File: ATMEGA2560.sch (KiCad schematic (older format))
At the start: 3 parts

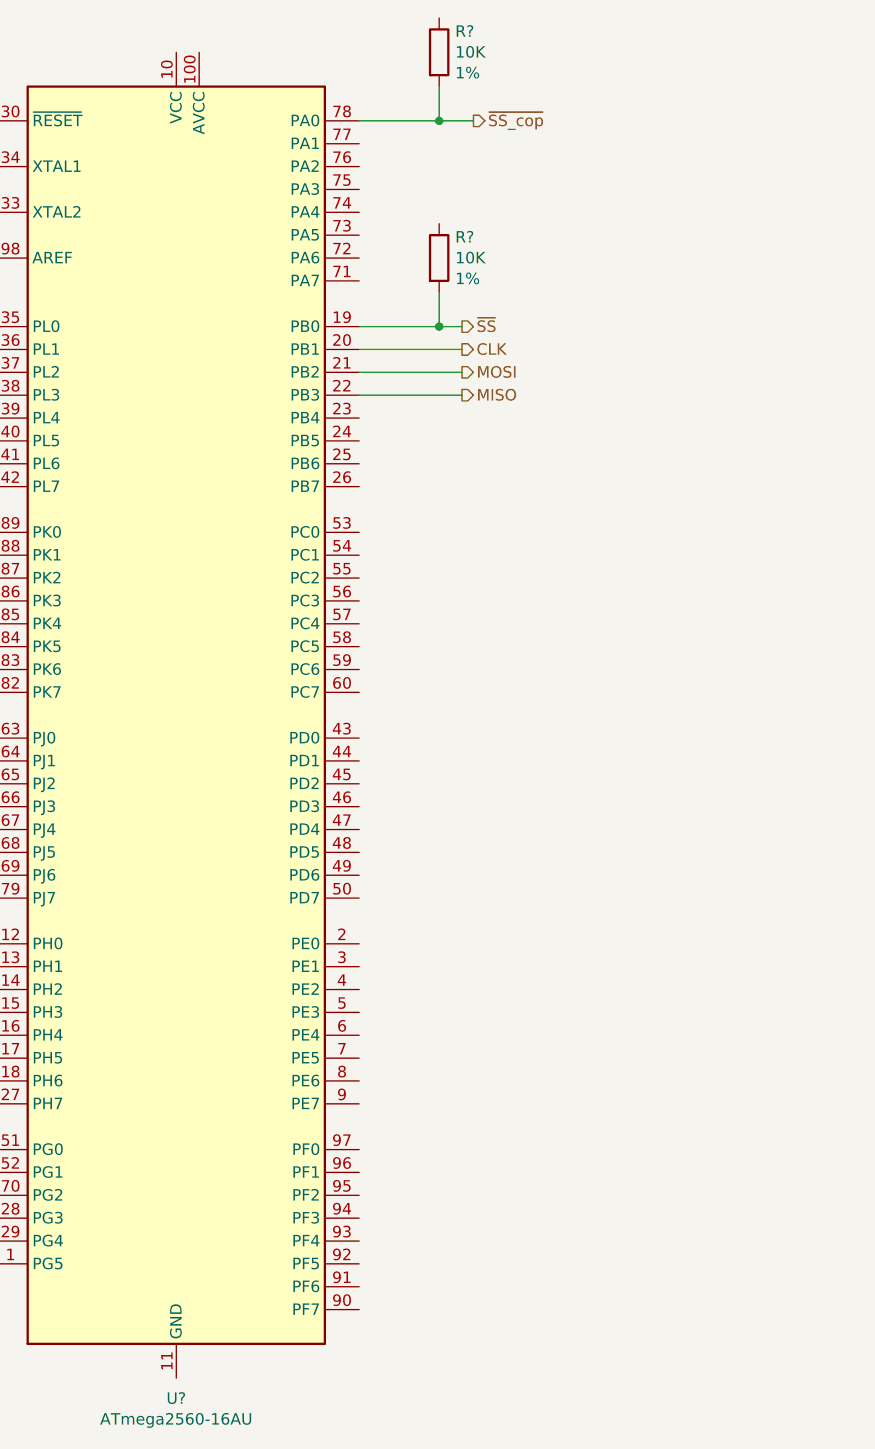
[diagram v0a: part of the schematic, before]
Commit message: Added all stepper circuits. Adding SPI bus to top level sheet. Opened up layout to check connectivity. Errors with footprint libs
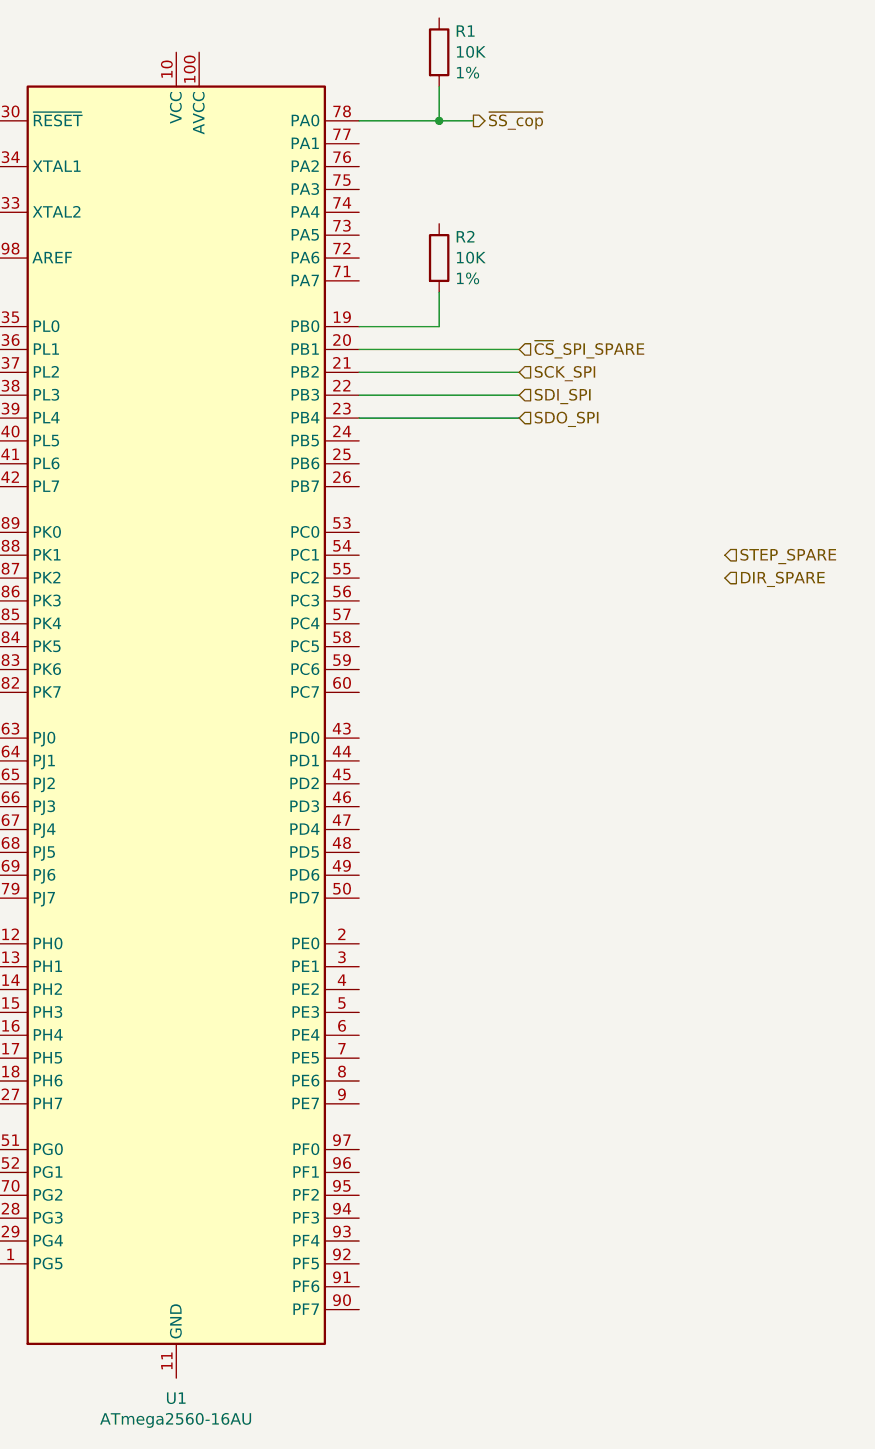
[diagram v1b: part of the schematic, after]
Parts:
- gave numbers to parts that had none: 3
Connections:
- net SDO_SPI: now reaches U1.23 (PB4)
- net CLK renamed ~CS~_SPI_SPARE
- net MISO renamed SDI_SPI
- net MOSI renamed SCK_SPI
- net ~SS: no longer names the net of R2.2, U1.19 (PB0)
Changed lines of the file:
@@
 EESchema Schematic File Version 4
-LIBS:bountifulHarvest-cache
-EELAYER 26 0
+EELAYER 30 0
 EELAYER END
 $Descr A4 11693 8268
 encoding utf-8
-Sheet 2 6
+Sheet 2 7
 Title ""
 Date ""
@@
 $EndDescr
 $Comp
-L bountifulHarvest-rescue:ATmega2560-16AU-MCU_Microchip_ATmega U?
+L bountifulHarvest-rescue:ATmega2560-16AU-MCU_Microchip_ATmega U1
 U 1 1 5EE66806
 P 4500 4250
-F 0 "U?" H 4500 1261 50  0000 C CNN
+F 0 "U1" H 4500 1261 50  0000 C CNN
 F 1 "ATmega2560-16AU" H 4500 1170 50  0000 C CNN
 F 2 "Package_QFP:TQFP-100_14x14mm_P0.5mm" H 4500 4250 50  0001 C CIN
@@
 	5300 1650 5650 1650
 $Comp
-L Device:R R?
+L Device:R R1
 U 1 1 5EE73D0C
 P 5650 1350
-F 0 "R?" H 5720 1441 50  0000 L CNN
+F 0 "R1" H 5720 1441 50  0000 L CNN
 F 1 "10K" H 5720 1350 50  0000 L CNN
 F 2 "" V 5580 1350 50  0001 C CNN
@@
 Wire Wire Line
 	5650 1650 5800 1650
-Text HLabel 5750 2850 2    50   Output ~ 0
-MISO
-Text HLabel 5750 2750 2    50   Output ~ 0
-MOSI
-Text HLabel 5750 2650 2    50   Output ~ 0
-CLK
-Text HLabel 5750 2550 2    50   Output ~ 0
-~SS
 $Comp
-L Device:R R?
+L Device:R R2
 U 1 1 5EE7AE50
 P 5650 2250
-F 0 "R?" H 5720 2341 50  0000 L CNN
+F 0 "R2" H 5720 2341 50  0000 L CNN
 F 1 "10K" H 5720 2250 50  0000 L CNN
 F 2 "" V 5580 2250 50  0001 C CNN
@@
 	5300 2550 5650 2550
 Wire Wire Line
-	5300 2650 5750 2650
+	5650 2400 5650 2550
+Text HLabel 6000 2650 2    50   Input ~ 0
+~CS~_SPI_SPARE
+Text HLabel 6000 2750 2    50   Input ~ 0
+SCK_SPI
+Text HLabel 6000 2850 2    50   Input ~ 0
+SDI_SPI
+Text HLabel 6000 2950 2    50   Input ~ 0
+SDO_SPI
+Text HLabel 6900 3550 2    50   Input ~ 0
+STEP_SPARE
+Text HLabel 6900 3650 2    50   Input ~ 0
+DIR_SPARE
 Wire Wire Line
-	5300 2750 5750 2750
+	5300 2650 6000 2650
 Wire Wire Line
-	5300 2850 5750 2850
+	6000 2750 5300 2750
 Wire Wire Line
-	5650 2400 5650 2550
-Connection ~ 5650 2550
+	5300 2850 6000 2850
 Wire Wire Line
-	5650 2550 5750 2550
+	6000 2950 5300 2950
 $EndSCHEMATC

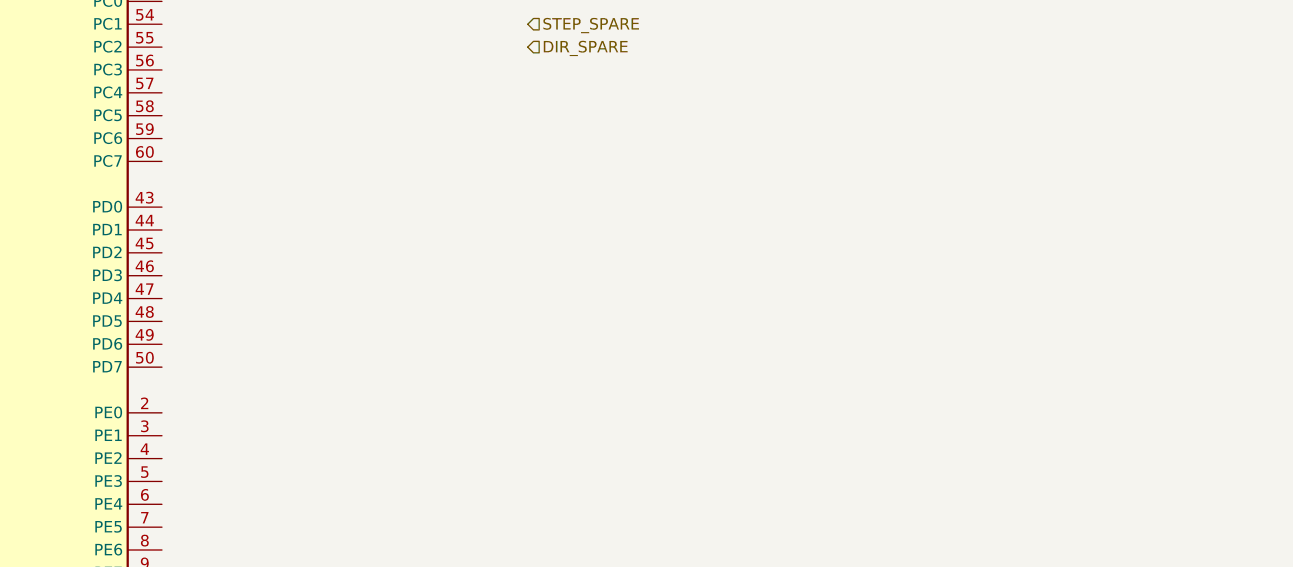
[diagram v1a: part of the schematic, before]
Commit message: Updated bus connections between drivers at ATMega
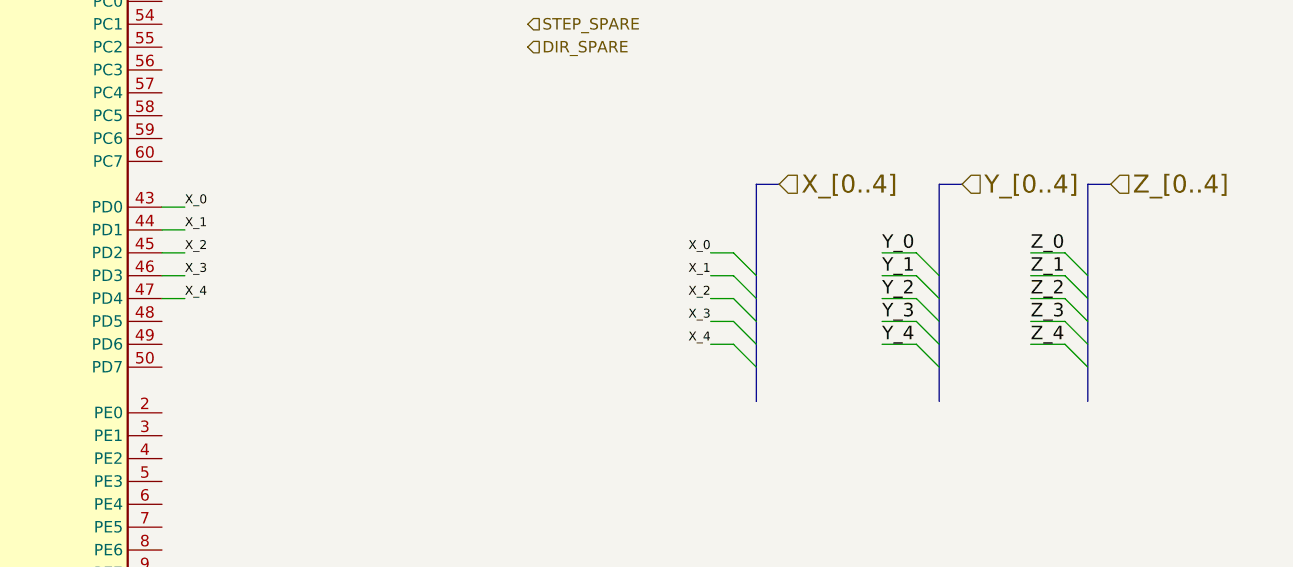
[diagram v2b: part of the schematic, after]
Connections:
- net X_0: now reaches U1.43 (PD0)
- net X_1: now reaches U1.44 (PD1)
- net X_2: now reaches U1.45 (PD2)
- net X_3: now reaches U1.46 (PD3)
- net X_4: now reaches U1.47 (PD4)
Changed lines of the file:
@@
 EESchema Schematic File Version 4
-EELAYER 30 0
+LIBS:bountifulHarvest-cache
+EELAYER 26 0
 EELAYER END
 $Descr A4 11693 8268
 encoding utf-8
-Sheet 2 7
+Sheet 6 7
 Title ""
 Date ""
@@
 Wire Wire Line
 	6000 2950 5300 2950
+Wire Wire Line
+	7700 4550 7800 4550
+Wire Wire Line
+	7700 4650 7800 4650
+Wire Wire Line
+	7700 4750 7800 4750
+Wire Wire Line
+	7700 4850 7800 4850
+Wire Wire Line
+	7700 4950 7800 4950
+Text Label 7700 4550 2    39   ~ 0
+X_0
+Text Label 7700 4650 2    39   ~ 0
+X_1
+Text Label 7700 4750 2    39   ~ 0
+X_2
+Text Label 7700 4850 2    39   ~ 0
+X_3
+Text Label 7700 4950 2    39   ~ 0
+X_4
+Entry Wire Line
+	7800 4550 7900 4650
+Entry Wire Line
+	7800 4650 7900 4750
+Entry Wire Line
+	7800 4750 7900 4850
+Entry Wire Line
+	7800 4850 7900 4950
+Entry Wire Line
+	7800 4950 7900 5050
+Wire Bus Line
+	7900 4250 8000 4250
+Wire Wire Line
+	5400 4350 5300 4350
+Wire Wire Line
+	5400 4450 5300 4450
+Wire Wire Line
+	5400 4550 5300 4550
+Wire Wire Line
+	5400 4650 5300 4650
+Wire Wire Line
+	5400 4750 5300 4750
+Text Label 5400 4350 0    39   ~ 0
+X_0
+Text Label 5400 4450 0    39   ~ 0
+X_1
+Text Label 5400 4550 0    39   ~ 0
+X_2
+Text Label 5400 4650 0    39   ~ 0
+X_3
+Text Label 5400 4750 0    39   ~ 0
+X_4
+Text HLabel 8000 4250 2    79   Input ~ 0
+X_[0..4]
+Entry Wire Line
+	8600 4550 8700 4650
+Entry Wire Line
+	8600 4650 8700 4750
+Entry Wire Line
+	8600 4750 8700 4850
+Entry Wire Line
+	8600 4850 8700 4950
+Entry Wire Line
+	8600 4950 8700 5050
+Text HLabel 8800 4250 2    79   Input ~ 0
+Y_[0..4]
+Wire Bus Line
+	8700 4250 8800 4250
+Entry Wire Line
+	9250 4550 9350 4650
+Entry Wire Line
+	9250 4650 9350 4750
+Entry Wire Line
+	9250 4750 9350 4850
+Entry Wire Line
+	9250 4850 9350 4950
+Entry Wire Line
+	9250 4950 9350 5050
+Text HLabel 9450 4250 2    79   Input ~ 0
+Z_[0..4]
+Wire Bus Line
+	9350 4250 9450 4250
+Text Label 8450 4550 0    59   ~ 0
+Y_0
+Text Label 8450 4650 0    59   ~ 0
+Y_1
+Text Label 8450 4750 0    59   ~ 0
+Y_2
+Text Label 8450 4850 0    59   ~ 0
+Y_3
+Text Label 8450 4950 0    59   ~ 0
+Y_4
+Wire Wire Line
+	8600 4550 8450 4550
+Wire Wire Line
+	8600 4650 8450 4650
+Wire Wire Line
+	8600 4750 8450 4750
+Wire Wire Line
+	8600 4850 8450 4850
+Wire Wire Line
+	8600 4950 8450 4950
+Text Label 9100 4550 0    59   ~ 0
+Z_0
+Text Label 9100 4650 0    59   ~ 0
+Z_1
+Text Label 9100 4750 0    59   ~ 0
+Z_2
+Text Label 9100 4850 0    59   ~ 0
+Z_3
+Text Label 9100 4950 0    59   ~ 0
+Z_4
+Wire Wire Line
+	9100 4550 9250 4550
+Wire Wire Line
+	9100 4650 9250 4650
+Wire Wire Line
+	9100 4750 9250 4750
+Wire Wire Line
+	9100 4850 9250 4850
+Wire Wire Line
+	9100 4950 9250 4950
+Wire Bus Line
+	7900 4250 7900 5200
+Wire Bus Line
+	8700 4250 8700 5200
+Wire Bus Line
+	9350 4250 9350 5200
 $EndSCHEMATC

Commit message: Fixed X,Y,Z driver bus connection. set up spare and X2
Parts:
- U1: Manufacturer P/N (none) -> ATMEGA2560-16AUR; Vendor P/N (none) -> ATMEGA2560-16AURCT-ND
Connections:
- net labels removed: DIR_SPARE, STEP_SPARE, ~CS~_SPI_SPARE
- wire segments 29 -> 38
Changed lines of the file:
@@
 $Descr A4 11693 8268
 encoding utf-8
-Sheet 6 7
+Sheet 5 7
 Title ""
 Date ""
@@
 F 2 "Package_QFP:TQFP-100_14x14mm_P0.5mm" H 4500 4250 50  0001 C CIN
 F 3 "http://ww1.microchip.com/downloads/en/DeviceDoc/Atmel-2549-8-bit-AVR-Microcontroller-ATmega640-1280-1281-2560-2561_datasheet.pdf" H 4500 4250 50  0001 C CNN
+F 4 "ATMEGA2560-16AUR" H 4500 4250 50  0001 C CNN "Manufacturer P/N"
+F 5 "ATMEGA2560-16AURCT-ND" H 4500 4250 50  0001 C CNN "Vendor P/N"
 	1    4500 4250
 	1    0    0    -1
@@
 Wire Wire Line
 	5650 2400 5650 2550
-Text HLabel 6000 2650 2    50   Input ~ 0
-~CS~_SPI_SPARE
 Text HLabel 6000 2750 2    50   Input ~ 0
 SCK_SPI
@@
 Text HLabel 6000 2950 2    50   Input ~ 0
 SDO_SPI
-Text HLabel 6900 3550 2    50   Input ~ 0
-STEP_SPARE
-Text HLabel 6900 3650 2    50   Input ~ 0
-DIR_SPARE
-Wire Wire Line
-	5300 2650 6000 2650
 Wire Wire Line
 	6000 2750 5300 2750
@@
 Wire Wire Line
 	6000 2950 5300 2950
-Wire Wire Line
-	7700 4550 7800 4550
-Wire Wire Line
-	7700 4650 7800 4650
-Wire Wire Line
-	7700 4750 7800 4750
-Wire Wire Line
-	7700 4850 7800 4850
-Wire Wire Line
-	7700 4950 7800 4950
-Text Label 7700 4550 2    39   ~ 0
+Text Label 600  850  2    39   ~ 0
 X_0
-Text Label 7700 4650 2    39   ~ 0
+Text Label 600  950  2    39   ~ 0
 X_1
-Text Label 7700 4750 2    39   ~ 0
+Text Label 600  1050 2    39   ~ 0
 X_2
-Text Label 7700 4850 2    39   ~ 0
+Text Label 600  1150 2    39   ~ 0
 X_3
-Text Label 7700 4950 2    39   ~ 0
+Text Label 600  1250 2    39   ~ 0
 X_4
 Entry Wire Line
-	7800 4550 7900 4650
-Entry Wire Line
-	7800 4650 7900 4750
-Entry Wire Line
-	7800 4750 7900 4850
-Entry Wire Line
-	7800 4850 7900 4950
-Entry Wire Line
-	7800 4950 7900 5050
-Wire Bus Line
-	7900 4250 8000 4250
-Wire Wire Line
-	5400 4350 5300 4350
-Wire Wire Line
-	5400 4450 5300 4450
-Wire Wire Line
-	5400 4550 5300 4550
-Wire Wire Line
-	5400 4650 5300 4650
-Wire Wire Line
-	5400 4750 5300 4750
-Text Label 5400 4350 0    39   ~ 0
+	900  850  1000 950
+Entry Wire Line
+	900  950  1000 1050
+Entry Wire Line
+	900  1050 1000 1150
+Entry Wire Line
+	900  1150 1000 1250
+Entry Wire Line
+	900  1250 1000 1350
+Wire Bus Line
+	1000 550  1100 550
+Text HLabel 1100 550  2    79   Input ~ 0
+X_[0..4]
+Entry Wire Line
+	1600 850  1700 950
+Entry Wire Line
+	1600 950  1700 1050
+Entry Wire Line
+	1600 1050 1700 1150
+Entry Wire Line
+	1600 1150 1700 1250
+Entry Wire Line
+	1600 1250 1700 1350
+Text HLabel 1800 550  2    79   Input ~ 0
+Y_[0..4]
+Wire Bus Line
+	1700 550  1800 550
+Entry Wire Line
+	2250 850  2350 950
+Entry Wire Line
+	2250 950  2350 1050
+Entry Wire Line
+	2250 1050 2350 1150
+Entry Wire Line
+	2250 1150 2350 1250
+Entry Wire Line
+	2250 1250 2350 1350
+Text HLabel 2450 550  2    79   Input ~ 0
+Z_[0..4]
+Wire Bus Line
+	2350 550  2450 550
+Text Label 1450 850  0    59   ~ 0
+Y_0
+Text Label 1450 950  0    59   ~ 0
+Y_1
+Text Label 1450 1050 0    59   ~ 0
+Y_2
+Text Label 1450 1150 0    59   ~ 0
+Y_3
+Text Label 1450 1250 0    59   ~ 0
+Y_4
+Wire Wire Line
+	1600 850  1450 850
+Wire Wire Line
+	1600 950  1450 950
+Wire Wire Line
+	1600 1050 1450 1050
+Wire Wire Line
+	1600 1150 1450 1150
+Wire Wire Line
+	1600 1250 1450 1250
+Text Label 2100 850  0    59   ~ 0
+Z_0
+Text Label 2100 950  0    59   ~ 0
+Z_1
+Text Label 2100 1050 0    59   ~ 0
+Z_2
+Text Label 2100 1150 0    59   ~ 0
+Z_3
+Text Label 2100 1250 0    59   ~ 0
+Z_4
+Wire Wire Line
+	2100 850  2250 850
+Wire Wire Line
+	2100 950  2250 950
+Wire Wire Line
+	2100 1050 2250 1050
+Wire Wire Line
+	2100 1150 2250 1150
+Wire Wire Line
+	2100 1250 2250 1250
+Wire Wire Line
+	600  850  900  850
+Wire Wire Line
+	600  950  900  950
+Wire Wire Line
+	600  1050 900  1050
+Wire Wire Line
+	600  1150 900  1150
+Wire Wire Line
+	600  1250 900  1250
+Text Label 5850 4650 2    39   ~ 0
 X_0
-Text Label 5400 4450 0    39   ~ 0
+Text Label 5850 4750 2    39   ~ 0
 X_1
-Text Label 5400 4550 0    39   ~ 0
+Text Label 5850 4850 2    39   ~ 0
 X_2
-Text Label 5400 4650 0    39   ~ 0
+Text Label 5850 4950 2    39   ~ 0
 X_3
-Text Label 5400 4750 0    39   ~ 0
+Text Label 5850 5050 2    39   ~ 0
 X_4
-Text HLabel 8000 4250 2    79   Input ~ 0
-X_[0..4]
-Entry Wire Line
-	8600 4550 8700 4650
-Entry Wire Line
-	8600 4650 8700 4750
-Entry Wire Line
-	8600 4750 8700 4850
-Entry Wire Line
-	8600 4850 8700 4950
-Entry Wire Line
-	8600 4950 8700 5050
-Text HLabel 8800 4250 2    79   Input ~ 0
-Y_[0..4]
-Wire Bus Line
-	8700 4250 8800 4250
-Entry Wire Line
-	9250 4550 9350 4650
-Entry Wire Line
-	9250 4650 9350 4750
-Entry Wire Line
-	9250 4750 9350 4850
-Entry Wire Line
-	9250 4850 9350 4950
-Entry Wire Line
-	9250 4950 9350 5050
-Text HLabel 9450 4250 2    79   Input ~ 0
-Z_[0..4]
-Wire Bus Line
-	9350 4250 9450 4250
-Text Label 8450 4550 0    59   ~ 0
+Wire Wire Line
+	5300 4650 5950 4650
+Wire Wire Line
+	5300 4750 5950 4750
+Wire Wire Line
+	5300 4850 5950 4850
+Wire Wire Line
+	5300 4950 5950 4950
+Wire Wire Line
+	5300 5050 5950 5050
+Text Label 5450 5250 0    59   ~ 0
 Y_0
-Text Label 8450 4650 0    59   ~ 0
+Text Label 5450 5350 0    59   ~ 0
 Y_1
-Text Label 8450 4750 0    59   ~ 0
+Text Label 5450 5450 0    59   ~ 0
 Y_2
-Text Label 8450 4850 0    59   ~ 0
+Text Label 5450 5550 0    59   ~ 0
 Y_3
-Text Label 8450 4950 0    59   ~ 0
+Text Label 5450 5650 0    59   ~ 0
 Y_4
 Wire Wire Line
-	8600 4550 8450 4550
-Wire Wire Line
-	8600 4650 8450 4650
-Wire Wire Line
-	8600 4750 8450 4750
-Wire Wire Line
-	8600 4850 8450 4850
-Wire Wire Line
-	8600 4950 8450 4950
-Text Label 9100 4550 0    59   ~ 0
+	5300 5250 5600 5250
+Text Label 3300 5250 0    59   ~ 0
 Z_0
-Text Label 9100 4650 0    59   ~ 0
+Text Label 3300 5350 0    59   ~ 0
 Z_1
-Text Label 9100 4750 0    59   ~ 0
+Text Label 3300 5450 0    59   ~ 0
 Z_2
-Text Label 9100 4850 0    59   ~ 0
+Text Label 3300 5550 0    59   ~ 0
 Z_3
-Text Label 9100 4950 0    59   ~ 0
+Text Label 3300 5650 0    59   ~ 0
 Z_4
 Wire Wire Line
-	9100 4550 9250 4550
-Wire Wire Line
-	9100 4650 9250 4650
-Wire Wire Line
-	9100 4750 9250 4750
-Wire Wire Line
-	9100 4850 9250 4850
-Wire Wire Line
-	9100 4950 9250 4950
-Wire Bus Line
-	7900 4250 7900 5200
-Wire Bus Line
-	8700 4250 8700 5200
-Wire Bus Line
-	9350 4250 9350 5200
+	5300 5350 5600 5350
+Wire Wire Line
+	5300 5450 5600 5450
+Wire Wire Line
+	5300 5550 5600 5550
+Wire Wire Line
+	5300 5650 5600 5650
+Wire Wire Line
+	3300 5250 3700 5250
+Wire Wire Line
+	3300 5350 3700 5350
+Wire Wire Line
+	3300 5450 3700 5450
+Wire Wire Line
+	3300 5550 3700 5550
+Wire Wire Line
+	3300 5650 3700 5650
+Wire Bus Line
+	1000 550  1000 1500
+Wire Bus Line
+	1700 550  1700 1500
+Wire Bus Line
+	2350 550  2350 1500
 $EndSCHEMATC
